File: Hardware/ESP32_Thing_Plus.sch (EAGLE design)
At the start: 56 parts, among them J3 QWIIC_RIGHT_ANGLE, J6 microSD, Q2 MBT3904DW1T1, Q3 20V/4.2A/52mΩ/1.4W, U1 MCP73831, U2 ESP-WROOM-32NARROW, U3 AP2112K-3.3, U4 MAX17048, U5 AP2112K-3.3, U6 THINGPLUS_LOGICAL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

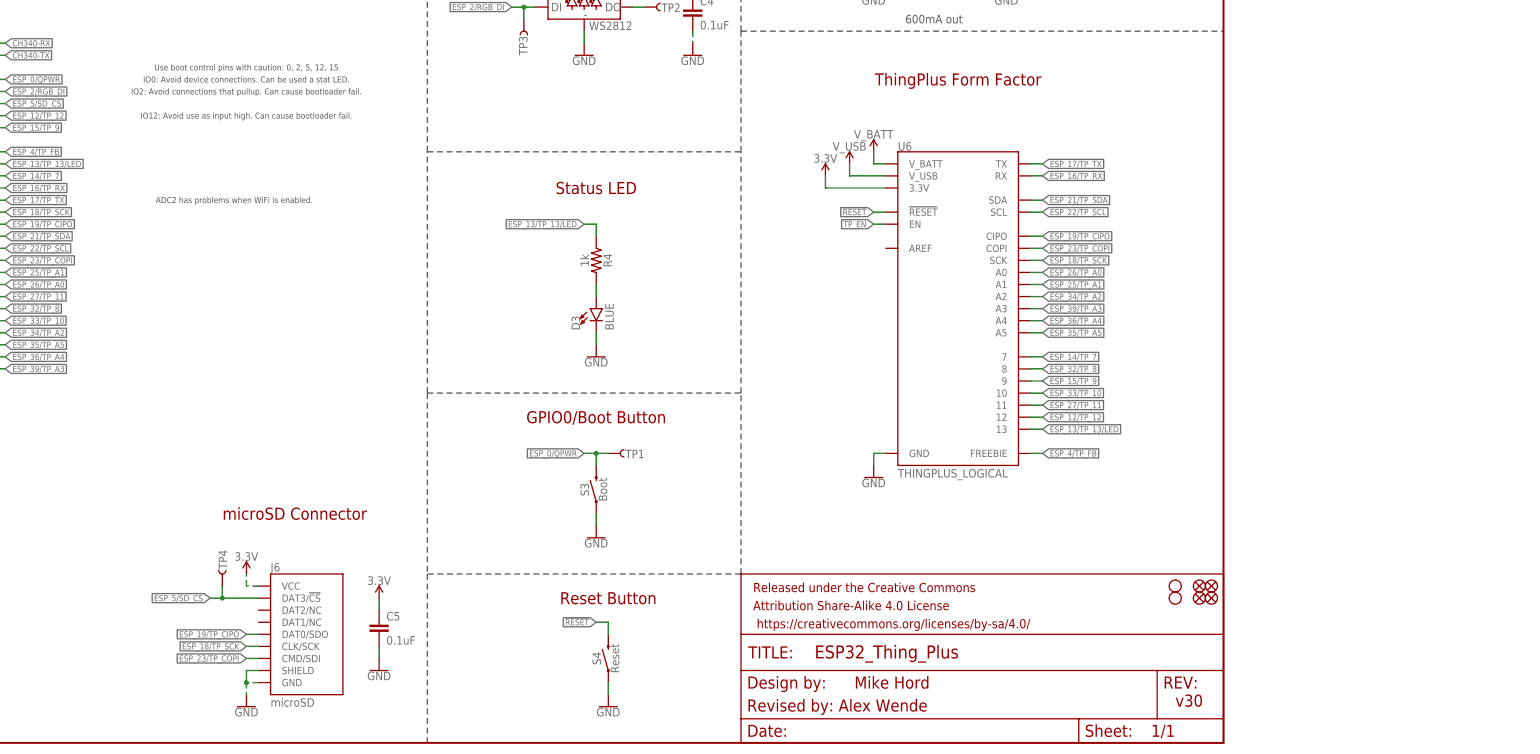
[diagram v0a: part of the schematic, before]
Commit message: Add test sketches
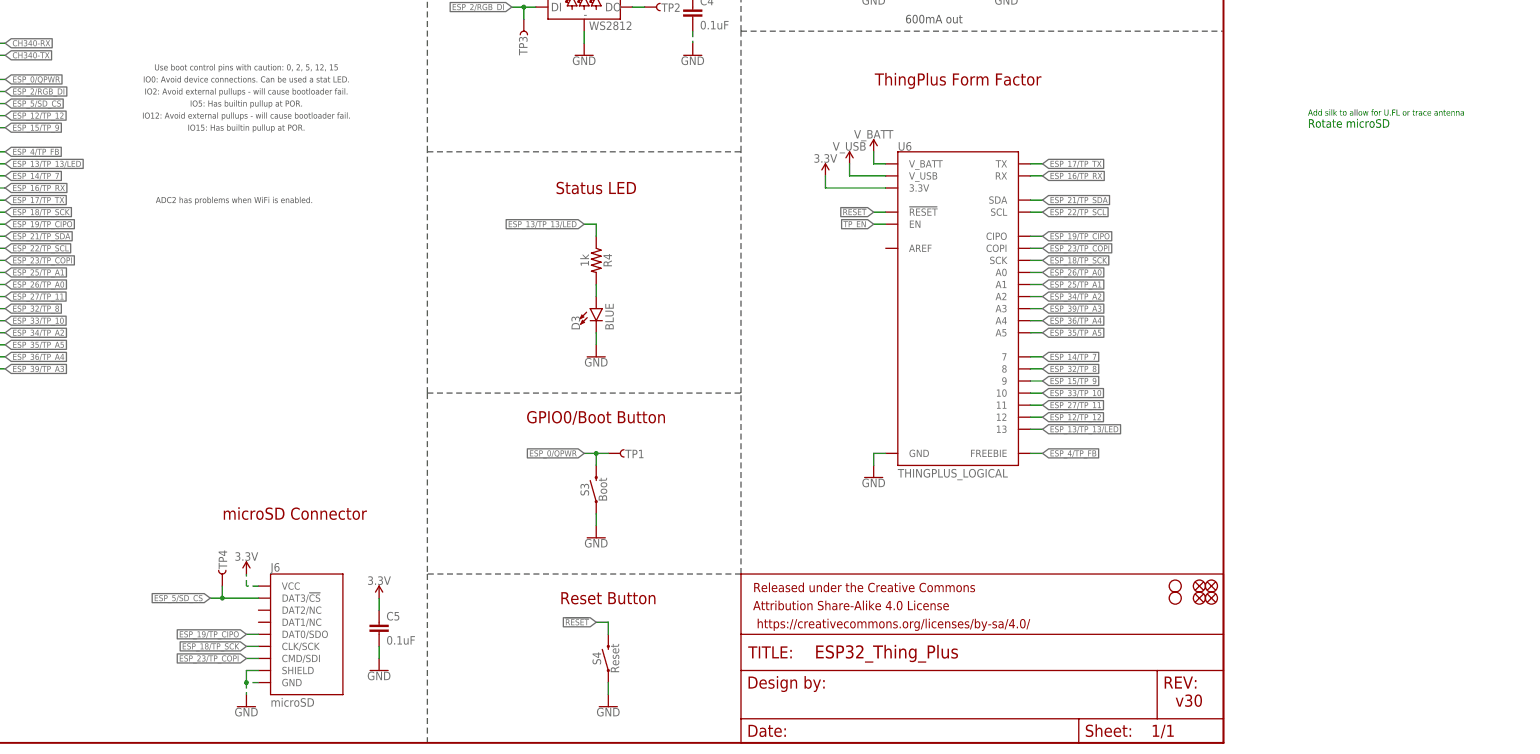
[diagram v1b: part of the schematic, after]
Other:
- note added: "Add silk to allow for U.FL or trace antenna"
- note added: "IO12: Avoid external pullups - will cause bootloader fail."
- note added: "IO15: Has builtin pullup at POR."
- note added: "IO2: Avoid external pullups - will cause bootloader fail."
- note added: "IO5: Has builtin pullup at POR."
- note added: "Rotate microSD"
- note removed: "IO12: Avoid use as input high. Can cause bootloader fail."
- note removed: "IO2: Avoid connections that pullup. Can cause bootloader fail."
- note removed: "Mike Hord"
- note removed: "Revised by: Alex Wende"
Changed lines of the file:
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@@
 <text x="381" y="187.96" size="2.54" layer="94" font="vector" align="center">Qwiic Connector</text>
 <wire x1="264.16" y1="73.66" x2="264.16" y2="124.46" width="0.1524" layer="97" style="longdash"/>
-<text x="354.076" y="11.43" size="2.54" layer="94">Mike Hord</text>
 <text x="299.72" y="116.84" size="2.54" layer="94" font="vector" align="center">Status LED</text>
 <wire x1="264.16" y1="124.46" x2="264.16" y2="193.04" width="0.1524" layer="97" style="longdash"/>
 <wire x1="264.16" y1="73.66" x2="264.16" y2="35.56" width="0.1524" layer="97" style="longdash"/>
 <text x="299.72" y="68.58" size="2.54" layer="94" align="center">GPIO0/Boot Button</text>
-<text x="331.47" y="6.604" size="2.54" layer="94">Revised by: Alex Wende</text>
 <text x="20.32" y="208.28" size="1.778" layer="97">V_USB - 6V MAX
 V_BATT - Single Cell (4.2V MAX)</text>
@@
 <text x="226.06" y="139.7" size="1.27" layer="97" align="center">IO0: Avoid device connections. Can be used a stat LED.</text>
 <text x="223.52" y="114.3" size="1.27" layer="97" align="center">ADC2 has problems when WiFi is enabled.</text>
-<text x="226.06" y="132.08" size="1.27" layer="97" align="center">IO12: Avoid use as input high. Can cause bootloader fail.</text>
+<text x="226.06" y="132.08" size="1.27" layer="97" align="center">IO12: Avoid external pullups - will cause bootloader fail.</text>
 <text x="226.06" y="142.24" size="1.27" layer="97" align="center">Use boot control pins with caution: 0, 2, 5, 12, 15</text>
-<text x="226.06" y="137.16" size="1.27" layer="97" align="center">IO2: Avoid connections that pullup. Can cause bootloader fail.</text>
+<text x="226.06" y="137.16" size="1.27" layer="97" align="center">IO2: Avoid external pullups - will cause bootloader fail.</text>
 <wire x1="330.2" y1="149.86" x2="431.8" y2="149.86" width="0.2032" layer="97" style="longdash"/>
 <text x="388.62" y="256.54" size="2.54" layer="94" font="vector" align="center">Fuel Gauge</text>
@@
 <text x="299.72" y="177.8" size="2.54" layer="94" font="vector" align="center">RGB Status LED</text>
 <text x="236.22" y="48.26" size="2.54" layer="94" font="vector" align="center">microSD Connector</text>
+<text x="449.58" y="132.08" size="1.27" layer="91">Add silk to allow for U.FL or trace antenna</text>
+<text x="226.06" y="129.54" size="1.27" layer="97" align="center">IO15: Has builtin pullup at POR.</text>
+<text x="226.06" y="134.62" size="1.27" layer="97" align="center">IO5: Has builtin pullup at POR.</text>
+<text x="449.58" y="129.54" size="1.778" layer="91">Rotate microSD</text>
 </plain>
 <instances>
